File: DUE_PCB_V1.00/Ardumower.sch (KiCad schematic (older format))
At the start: 55 parts, among them J1 9V IN, J10 Sonar_R, J11 Sonar_C, J12 Sonar_L, J13 P_Right, J14 Buzzer, J15 Button, J16 US1, J17 US2, J18 US3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

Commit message: Add Pin Description on PCB
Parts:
- added J33: ReserveD8, Connector_PinHeader_2.54mm:PinHeader_1x02_P2.54mm_Vertical, symbol Connector:Screw_Terminal_01x02
- added J34: ReserveD9, Connector_PinHeader_2.54mm:PinHeader_1x02_P2.54mm_Vertical, symbol Connector:Screw_Terminal_01x02
- added J35: ReserveD49, Connector_PinHeader_2.54mm:PinHeader_1x02_P2.54mm_Vertical, symbol Connector:Screw_Terminal_01x02
- added J36: ReserveA10, Connector_PinHeader_2.54mm:PinHeader_1x02_P2.54mm_Vertical, symbol Connector:Screw_Terminal_01x02
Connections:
- net GND: now also J33.1 (Pin_1), J34.1 (Pin_1), J35.1 (Pin_1), J36.1 (Pin_1)
- net pinReserveA10: now also J36.2 (Pin_2)
- net pinReserveD49: now also J35.2 (Pin_2)
- net pinReserveD8: now also J33.2 (Pin_2)
- net pinReserveD9: now also J34.2 (Pin_2)
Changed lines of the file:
@@
 	0    -1   -1   0
 $EndComp
+Text GLabel 1100 4300 0    50   Input ~ 0
+pinReserveA10
+Text GLabel 1100 3250 0    50   Input ~ 0
+pinReserveD8
+Text GLabel 1100 3600 0    50   Input ~ 0
+pinReserveD9
+Text GLabel 1100 3950 0    50   Input ~ 0
+pinReserveD49
+$Comp
+L Connector:Screw_Terminal_01x02 J33
+U 1 1 60E9F79C
+P 1300 3150
+F 0 "J33" H 1380 3142 50  0000 L CNN
+F 1 "ReserveD8" H 1380 3051 50  0000 L CNN
+F 2 "Connector_PinHeader_2.54mm:PinHeader_1x02_P2.54mm_Vertical" H 1300 3150 50  0001 C CNN
+F 3 "~" H 1300 3150 50  0001 C CNN
+	1    1300 3150
+	1    0    0    -1
+$EndComp
+$Comp
+L power:GND #PWR052
+U 1 1 60EA02A5
+P 1100 3150
+F 0 "#PWR052" H 1100 2900 50  0001 C CNN
+F 1 "GND" V 1105 3022 50  0000 R CNN
+F 2 "" H 1100 3150 50  0001 C CNN
+F 3 "" H 1100 3150 50  0001 C CNN
+	1    1100 3150
+	0    1    1    0
+$EndComp
+$Comp
+L Connector:Screw_Terminal_01x02 J34
+U 1 1 60EA5E97
+P 1300 3500
+F 0 "J34" H 1380 3492 50  0000 L CNN
+F 1 "ReserveD9" H 1380 3401 50  0000 L CNN
+F 2 "Connector_PinHeader_2.54mm:PinHeader_1x02_P2.54mm_Vertical" H 1300 3500 50  0001 C CNN
+F 3 "~" H 1300 3500 50  0001 C CNN
+	1    1300 3500
+	1    0    0    -1
+$EndComp
+$Comp
+L power:GND #PWR059
+U 1 1 60EA5EA1
+P 1100 3500
+F 0 "#PWR059" H 1100 3250 50  0001 C CNN
+F 1 "GND" V 1105 3372 50  0000 R CNN
+F 2 "" H 1100 3500 50  0001 C CNN
+F 3 "" H 1100 3500 50  0001 C CNN
+	1    1100 3500
+	0    1    1    0
+$EndComp
+$Comp
+L Connector:Screw_Terminal_01x02 J35
+U 1 1 60EA806D
+P 1300 3850
+F 0 "J35" H 1380 3842 50  0000 L CNN
+F 1 "ReserveD49" H 1380 3751 50  0000 L CNN
+F 2 "Connector_PinHeader_2.54mm:PinHeader_1x02_P2.54mm_Vertical" H 1300 3850 50  0001 C CNN
+F 3 "~" H 1300 3850 50  0001 C CNN
+	1    1300 3850
+	1    0    0    -1
+$EndComp
+$Comp
+L power:GND #PWR062
+U 1 1 60EA8077
+P 1100 3850
+F 0 "#PWR062" H 1100 3600 50  0001 C CNN
+F 1 "GND" V 1105 3722 50  0000 R CNN
+F 2 "" H 1100 3850 50  0001 C CNN
+F 3 "" H 1100 3850 50  0001 C CNN
+	1    1100 3850
+	0    1    1    0
+$EndComp
+$Comp
+L Connector:Screw_Terminal_01x02 J36
+U 1 1 60EA8082
+P 1300 4200
+F 0 "J36" H 1380 4192 50  0000 L CNN
+F 1 "ReserveA10" H 1380 4101 50  0000 L CNN
+F 2 "Connector_PinHeader_2.54mm:PinHeader_1x02_P2.54mm_Vertical" H 1300 4200 50  0001 C CNN
+F 3 "~" H 1300 4200 50  0001 C CNN
+	1    1300 4200
+	1    0    0    -1
+$EndComp
+$Comp
+L power:GND #PWR065
+U 1 1 60EA808C
+P 1100 4200
+F 0 "#PWR065" H 1100 3950 50  0001 C CNN
+F 1 "GND" V 1105 4072 50  0000 R CNN
+F 2 "" H 1100 4200 50  0001 C CNN
+F 3 "" H 1100 4200 50  0001 C CNN
+	1    1100 4200
+	0    1    1    0
+$EndComp
 $EndSCHEMATC

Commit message: Add Motor Connectors
Add Default Motor Connectors and reorder Ser0-Ser3
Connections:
- net +3V3: now also J22.2 (Pin_2), J23.2 (Pin_2), J24.2 (Pin_2), J31.2 (Pin_2); no longer J22.4 (Pin_4), J23.4 (Pin_4), J24.4 (Pin_4), J31.4 (Pin_4)
- net GND: now also J22.3 (Pin_3), J23.3 (Pin_3), J24.3 (Pin_3), J31.3 (Pin_3); no longer J22.5 (Pin_5), J23.5 (Pin_5), J24.5 (Pin_5), J31.5 (Pin_5)
- net RX0: now also J22.5 (Pin_5); no longer J22.3 (Pin_3)
- net RX1: now also J23.5 (Pin_5); no longer J23.3 (Pin_3)
- net RX2: now also J24.5 (Pin_5); no longer J24.3 (Pin_3)
- net RX3: now also J31.5 (Pin_5); no longer J31.3 (Pin_3)
- net TX0: now also J22.4 (Pin_4); no longer J22.2 (Pin_2)
- net TX1: now also J23.4 (Pin_4); no longer J23.2 (Pin_2)
- net TX2: now also J24.4 (Pin_4); no longer J24.2 (Pin_2)
- net TX3: now also J31.4 (Pin_4); no longer J31.2 (Pin_2)
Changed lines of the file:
@@
 Text GLabel 4850 4200 0    50   Input ~ 0
 pinReserveA10
-Text GLabel 9000 6250 0    50   Input ~ 0
+Text GLabel 9000 6450 0    50   Input ~ 0
 RX1
-Text GLabel 9000 6150 0    50   Output ~ 0
+Text GLabel 9000 6350 0    50   Output ~ 0
 TX1
 $Comp
@@
 L power:+3.3V #PWR073
 U 1 1 60D8E37F
-P 9000 6350
-F 0 "#PWR073" H 9000 6200 50  0001 C CNN
-F 1 "+3.3V" V 9015 6478 50  0000 L CNN
-F 2 "" H 9000 6350 50  0001 C CNN
-F 3 "" H 9000 6350 50  0001 C CNN
-	1    9000 6350
+P 9000 6150
+F 0 "#PWR073" H 9000 6000 50  0001 C CNN
+F 1 "+3.3V" V 9015 6278 50  0000 L CNN
+F 2 "" H 9000 6150 50  0001 C CNN
+F 3 "" H 9000 6150 50  0001 C CNN
+	1    9000 6150
 	0    -1   -1   0
 $EndComp
@@
 L power:GND #PWR074
 U 1 1 60D8F6A0
-P 9000 6450
-F 0 "#PWR074" H 9000 6200 50  0001 C CNN
-F 1 "GND" V 9005 6322 50  0000 R CNN
-F 2 "" H 9000 6450 50  0001 C CNN
-F 3 "" H 9000 6450 50  0001 C CNN
-	1    9000 6450
+P 9000 6250
+F 0 "#PWR074" H 9000 6000 50  0001 C CNN
+F 1 "GND" V 9005 6122 50  0000 R CNN
+F 2 "" H 9000 6250 50  0001 C CNN
+F 3 "" H 9000 6250 50  0001 C CNN
+	1    9000 6250
 	0    1    1    0
 $EndComp
@@
 	0    -1   -1   0
 $EndComp
-Text GLabel 9900 6250 0    50   Input ~ 0
+Text GLabel 9900 6450 0    50   Input ~ 0
 RX2
-Text GLabel 9900 6150 0    50   Output ~ 0
+Text GLabel 9900 6350 0    50   Output ~ 0
 TX2
 $Comp
@@
 L power:+3.3V #PWR076
 U 1 1 60D92BA8
-P 9900 6350
-F 0 "#PWR076" H 9900 6200 50  0001 C CNN
-F 1 "+3.3V" V 9915 6478 50  0000 L CNN
-F 2 "" H 9900 6350 50  0001 C CNN
-F 3 "" H 9900 6350 50  0001 C CNN
-	1    9900 6350
+P 9900 6150
+F 0 "#PWR076" H 9900 6000 50  0001 C CNN
+F 1 "+3.3V" V 9915 6278 50  0000 L CNN
+F 2 "" H 9900 6150 50  0001 C CNN
+F 3 "" H 9900 6150 50  0001 C CNN
+	1    9900 6150
 	0    -1   -1   0
 $EndComp
@@
 L power:GND #PWR077
 U 1 1 60D92BB2
-P 9900 6450
-F 0 "#PWR077" H 9900 6200 50  0001 C CNN
-F 1 "GND" V 9905 6322 50  0000 R CNN
-F 2 "" H 9900 6450 50  0001 C CNN
-F 3 "" H 9900 6450 50  0001 C CNN
-	1    9900 6450
+P 9900 6250
+F 0 "#PWR077" H 9900 6000 50  0001 C CNN
+F 1 "GND" V 9905 6122 50  0000 R CNN
+F 2 "" H 9900 6250 50  0001 C CNN
+F 3 "" H 9900 6250 50  0001 C CNN
+	1    9900 6250
 	0    1    1    0
 $EndComp
@@
 	0    -1   -1   0
 $EndComp
-Text GLabel 8100 6250 0    50   Input ~ 0
+Text GLabel 8100 6450 0    50   Input ~ 0
 RX0
-Text GLabel 8100 6150 0    50   Output ~ 0
+Text GLabel 8100 6350 0    50   Output ~ 0
 TX0
 $Comp
@@
 L power:+3.3V #PWR045
 U 1 1 60D9F76A
-P 8100 6350
-F 0 "#PWR045" H 8100 6200 50  0001 C CNN
-F 1 "+3.3V" V 8115 6478 50  0000 L CNN
-F 2 "" H 8100 6350 50  0001 C CNN
-F 3 "" H 8100 6350 50  0001 C CNN
-	1    8100 6350
+P 8100 6150
+F 0 "#PWR045" H 8100 6000 50  0001 C CNN
+F 1 "+3.3V" V 8115 6278 50  0000 L CNN
+F 2 "" H 8100 6150 50  0001 C CNN
+F 3 "" H 8100 6150 50  0001 C CNN
+	1    8100 6150
 	0    -1   -1   0
 $EndComp
@@
 L power:GND #PWR071
 U 1 1 60D9F774
-P 8100 6450
-F 0 "#PWR071" H 8100 6200 50  0001 C CNN
-F 1 "GND" V 8105 6322 50  0000 R CNN
-F 2 "" H 8100 6450 50  0001 C CNN
-F 3 "" H 8100 6450 50  0001 C CNN
-	1    8100 6450
+P 8100 6250
+F 0 "#PWR071" H 8100 6000 50  0001 C CNN
+F 1 "GND" V 8105 6122 50  0000 R CNN
+F 2 "" H 8100 6250 50  0001 C CNN
+F 3 "" H 8100 6250 50  0001 C CNN
+	1    8100 6250
 	0    1    1    0
 $EndComp
@@
 	0    -1   -1   0
 $EndComp
-Text GLabel 10750 6250 0    50   Input ~ 0
+Text GLabel 10750 6450 0    50   Input ~ 0
 RX3
-Text GLabel 10750 6150 0    50   Output ~ 0
+Text GLabel 10750 6350 0    50   Output ~ 0
 TX3
 $Comp
@@
 L power:+3.3V #PWR079
 U 1 1 60DA6ECE
-P 10750 6350
-F 0 "#PWR079" H 10750 6200 50  0001 C CNN
-F 1 "+3.3V" V 10765 6478 50  0000 L CNN
-F 2 "" H 10750 6350 50  0001 C CNN
-F 3 "" H 10750 6350 50  0001 C CNN
-	1    10750 6350
+P 10750 6150
+F 0 "#PWR079" H 10750 6000 50  0001 C CNN
+F 1 "+3.3V" V 10765 6278 50  0000 L CNN
+F 2 "" H 10750 6150 50  0001 C CNN
+F 3 "" H 10750 6150 50  0001 C CNN
+	1    10750 6150
 	0    -1   -1   0
 $EndComp
@@
 L power:GND #PWR080
 U 1 1 60DA6ED8
-P 10750 6450
-F 0 "#PWR080" H 10750 6200 50  0001 C CNN
-F 1 "GND" V 10755 6322 50  0000 R CNN
-F 2 "" H 10750 6450 50  0001 C CNN
-F 3 "" H 10750 6450 50  0001 C CNN
-	1    10750 6450
-	0    1    1    0
-$EndComp
+P 10750 6250
+F 0 "#PWR080" H 10750 6000 50  0001 C CNN
+F 1 "GND" V 10755 6122 50  0000 R CNN
+F 2 "" H 10750 6250 50  0001 C CNN
+F 3 "" H 10750 6250 50  0001 C CNN
+	1    10750 6250
+	0    1    1    0
+$EndComp

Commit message: Drop Pin Summary
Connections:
- net +3V3: now also J21.6 (Pin_6)
- net pinVoltageMeasurement: no longer J21.6 (Pin_6)
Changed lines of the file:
@@
 Text GLabel 4700 7500 0    50   Output ~ 0
 pinChargeRelay
-Text GLabel 4700 7600 0    50   Input ~ 0
-pinVoltageMeasurement
 $Comp
 L Connector:Screw_Terminal_01x04 J20
@@
 	-1   0    0    1
 $EndComp
+$Comp
+L power:+3.3V #PWR?
+U 1 1 60B536A7
+P 4100 7600
+F 0 "#PWR?" H 4100 7450 50  0001 C CNN
+F 1 "+3.3V" V 4115 7728 50  0000 L CNN
+F 2 "" H 4100 7600 50  0001 C CNN
+F 3 "" H 4100 7600 50  0001 C CNN
+	1    4100 7600
+	0    -1   -1   0
+$EndComp
+Wire Wire Line
+	4100 7600 4700 7600
 $EndSCHEMATC

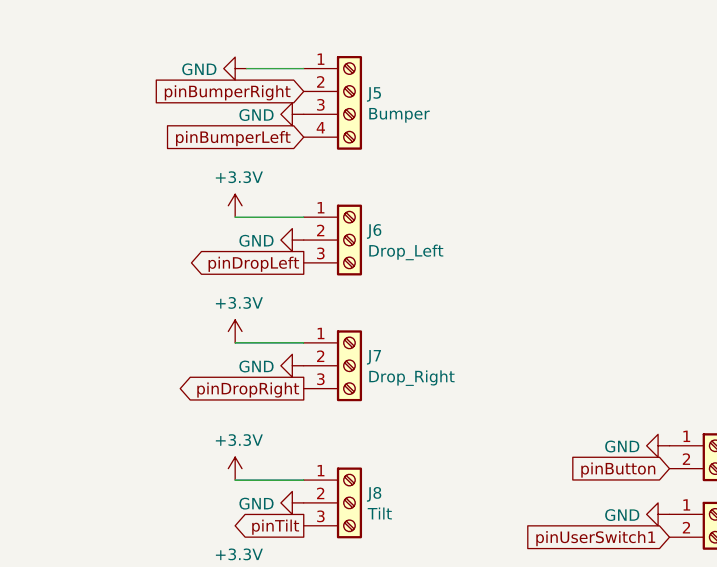
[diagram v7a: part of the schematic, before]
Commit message: Remove 24V from PCB
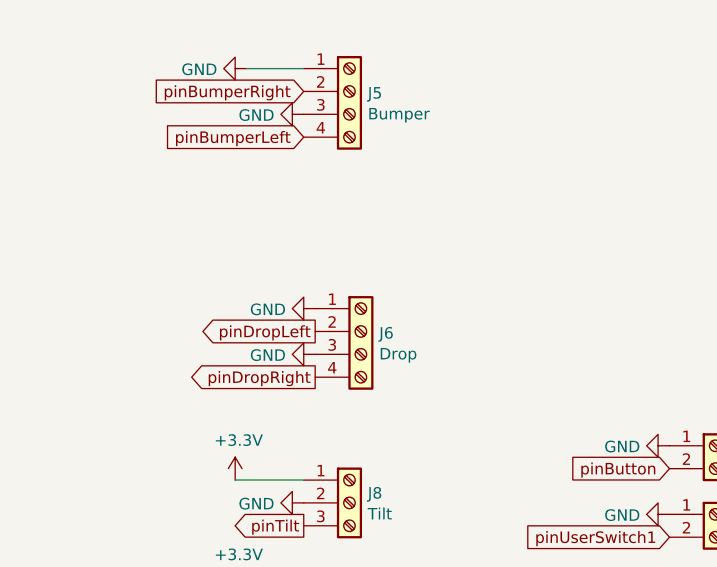
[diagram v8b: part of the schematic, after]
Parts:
- removed J6: Drop_Left, Connector_PinHeader_2.54mm:PinHeader_1x03_P2.54mm_Vertical, symbol Connector:Screw_Terminal_01x03
- removed J7: Drop_Right, Connector_PinHeader_2.54mm:PinHeader_1x03_P2.54mm_Vertical, symbol Connector:Screw_Terminal_01x03
- added J6: Drop, Connector_PinHeader_2.54mm:PinHeader_1x04_P2.54mm_Vertical, symbol Connector:Screw_Terminal_01x04
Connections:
- net GND: now also J6.1 (Pin_1), J6.3 (Pin_3)
- net pinDropLeft: now also J6.2 (Pin_2)
- net pinDropRight: now also J6.4 (Pin_4)
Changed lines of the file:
@@
 pinPerimeterRight
-$Comp
-L Connector:Screw_Terminal_01x03 J6
-U 1 1 60780996
-P 1650 5700
-F 0 "J6" H 1730 5742 50  0000 L CNN
-F 1 "Drop_Left" H 1730 5651 50  0000 L CNN
-F 2 "Connector_PinHeader_2.54mm:PinHeader_1x03_P2.54mm_Vertical" H 1650 5700 50  0001 C CNN
-F 3 "~" H 1650 5700 50  0001 C CNN
-	1    1650 5700
-	1    0    0    -1
-$EndComp
-$Comp
-L Connector:Screw_Terminal_01x03 J7
-U 1 1 6078194B
-P 1650 6250
-F 0 "J7" H 1730 6292 50  0000 L CNN
-F 1 "Drop_Right" H 1730 6201 50  0000 L CNN
-F 2 "Connector_PinHeader_2.54mm:PinHeader_1x03_P2.54mm_Vertical" H 1650 6250 50  0001 C CNN
-F 3 "~" H 1650 6250 50  0001 C CNN
-	1    1650 6250
-	1    0    0    -1
-$EndComp
-$Comp
-L power:+3.3V #PWR08
-U 1 1 607849F2
-P 1150 5600
-F 0 "#PWR08" H 1150 5450 50  0001 C CNN
-F 1 "+3.3V" H 1165 5773 50  0000 C CNN
-F 2 "" H 1150 5600 50  0001 C CNN
-F 3 "" H 1150 5600 50  0001 C CNN
-	1    1150 5600
-	1    0    0    -1
-$EndComp
-Wire Wire Line
-	1150 5600 1450 5600
-$Comp
-L power:+3.3V #PWR09
-U 1 1 60785E20
-P 1150 6150
-F 0 "#PWR09" H 1150 6000 50  0001 C CNN
-F 1 "+3.3V" H 1165 6323 50  0000 C CNN
-F 2 "" H 1150 6150 50  0001 C CNN
-F 3 "" H 1150 6150 50  0001 C CNN
-	1    1150 6150
-	1    0    0    -1
-$EndComp
-Wire Wire Line
-	1150 6150 1450 6150
-Text GLabel 1450 6350 0    50   Output ~ 0
-pinDropRight
-Text GLabel 1450 5800 0    50   Output ~ 0
-pinDropLeft
 $Comp
 L Connector:Screw_Terminal_01x03 J8
@@
 F 3 "" H 1450 6850 50  0001 C CNN
 	1    1450 6850
-	0    1    1    0
-$EndComp
-$Comp
-L power:GND #PWR015
-U 1 1 6097E7D6
-P 1450 6250
-F 0 "#PWR015" H 1450 6000 50  0001 C CNN
-F 1 "GND" V 1455 6122 50  0000 R CNN
-F 2 "" H 1450 6250 50  0001 C CNN
-F 3 "" H 1450 6250 50  0001 C CNN
-	1    1450 6250
-	0    1    1    0
-$EndComp
-$Comp
-L power:GND #PWR014
-U 1 1 6097E9D0
-P 1450 5700
-F 0 "#PWR014" H 1450 5450 50  0001 C CNN
-F 1 "GND" V 1455 5572 50  0000 R CNN
-F 2 "" H 1450 5700 50  0001 C CNN
-F 3 "" H 1450 5700 50  0001 C CNN
-	1    1450 5700
 	0    1    1    0
 $EndComp
@@
 $EndComp
 $Comp
-L power:+3.3V #PWR?
+L power:+3.3V #PWR08
 U 1 1 60B536A7
 P 4100 7600
-F 0 "#PWR?" H 4100 7450 50  0001 C CNN
+F 0 "#PWR08" H 4100 7450 50  0001 C CNN
 F 1 "+3.3V" V 4115 7728 50  0000 L CNN
 F 2 "" H 4100 7600 50  0001 C CNN
@@
 Wire Wire Line
 	4100 7600 4700 7600
+$Comp
+L Connector:Screw_Terminal_01x04 J6
+U 1 1 60B57732
+P 1700 6100
+F 0 "J6" H 1780 6092 50  0000 L CNN
+F 1 "Drop" H 1780 6001 50  0000 L CNN
+F 2 "Connector_PinHeader_2.54mm:PinHeader_1x04_P2.54mm_Vertical" H 1700 6100 50  0001 C CNN
+F 3 "~" H 1700 6100 50  0001 C CNN
+	1    1700 6100
+	1    0    0    -1
+$EndComp
+$Comp
+L power:GND #PWR014
+U 1 1 6097E9D0
+P 1500 6000
+F 0 "#PWR014" H 1500 5750 50  0001 C CNN
+F 1 "GND" V 1505 5872 50  0000 R CNN
+F 2 "" H 1500 6000 50  0001 C CNN
+F 3 "" H 1500 6000 50  0001 C CNN
+	1    1500 6000
+	0    1    1    0
+$EndComp
+$Comp
+L power:GND #PWR015
+U 1 1 6097E7D6
+P 1500 6200
+F 0 "#PWR015" H 1500 5950 50  0001 C CNN
+F 1 "GND" V 1505 6072 50  0000 R CNN
+F 2 "" H 1500 6200 50  0001 C CNN
+F 3 "" H 1500 6200 50  0001 C CNN
+	1    1500 6200
+	0    1    1    0
+$EndComp
+Text GLabel 1500 6100 0    50   Output ~ 0
+pinDropLeft
+Text GLabel 1500 6300 0    50   Output ~ 0
+pinDropRight
 $EndSCHEMATC
